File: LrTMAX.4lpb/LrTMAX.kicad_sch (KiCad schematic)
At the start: 126 parts, among them J1 USB_C_Receptacle_USB2.0, J2 Conn_02x05_Odd_Even, Q1 2N7002, SW1 Tact_SW_8mm, SW10 EC11_SMD, SW11 EC11_SMD, SW12 EC11_SMD, SW13 EC11_SMD, SW14 EC11_SMD, SW15 EC11_SMD, SW16 EC11_SMD, SW17 EC11_SMD, SW2 Tact_SW_8mm, SW3 Tact_SW_8mm, SW4 Tact_SW_8mm, SW5 Tact_SW_8mm, SW6 Tact_SW_8mm, SW7 Tact_SW_8mm, SW8 Tact_SW_8mm, U1 STM32F072C8Tx, U3 SSD1306_OLED_0.91, U4 SPX3819M5-L3-3TR

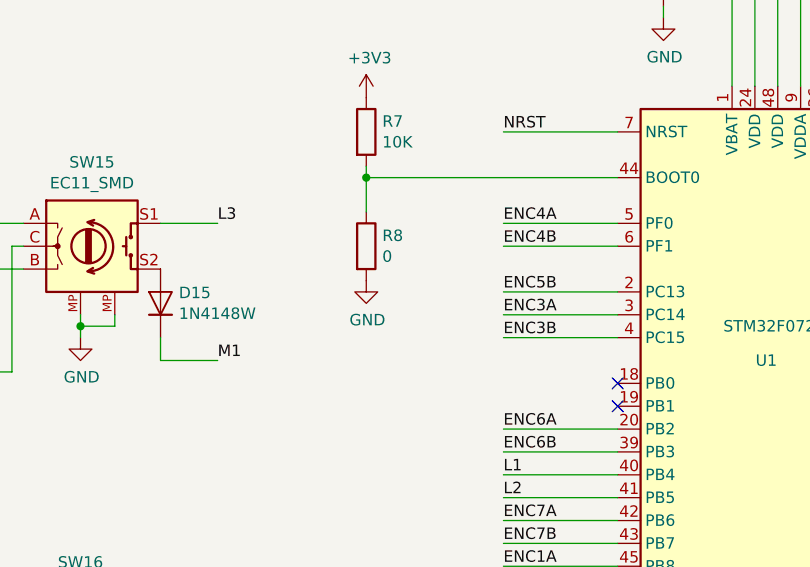
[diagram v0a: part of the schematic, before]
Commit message: Added DFU DIP Switch.
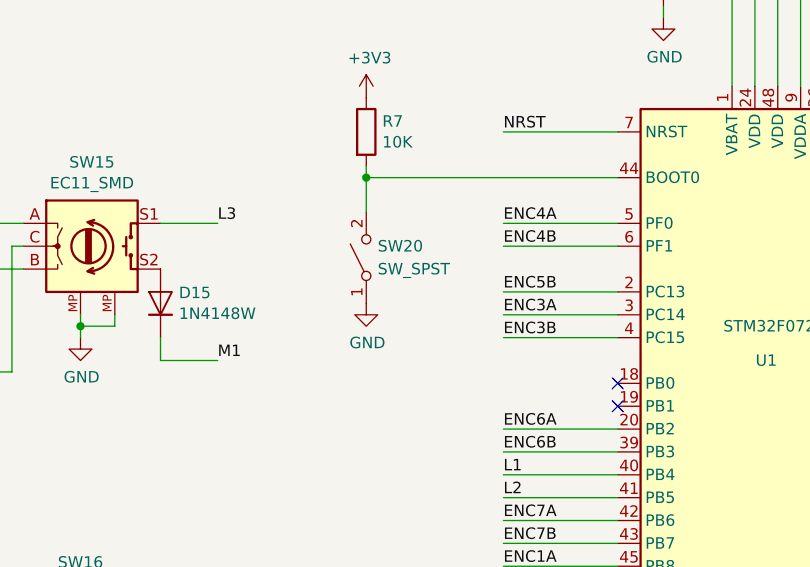
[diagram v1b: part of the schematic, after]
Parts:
- removed R8: 0, Resistor_SMD:R_0805_2012Metric, symbol Device:R
- added SW20: SW_SPST, Button_Switch_SMD:SW_DIP_SPSTx01_Slide_Copal_CHS-01B_W7.62mm_P1.27mm, symbol Switch:SW_SPST
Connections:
- net GND: now also SW20.1 (A)
- net at R7.2, U1.44 (BOOT0): now also SW20.2 (B)
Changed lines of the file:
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@@
     (pin "2")
   )
-  (symbol (lib_id "LrE-6-rescue:GND-power") (at 170.18 83.82 0) (unit 1)
-    (in_bom yes) (on_board yes)
-    (property "Reference" "#PWR0141" (id 0) (at 170.18 90.17 0)
-      (effects (font (size 1.27 1.27)) hide)
-    )
-    (property "Value" "GND" (id 1) (at 170.307 88.2142 0))
-    (property "Footprint" "" (id 2) (at 170.18 83.82 0)
-      (effects (font (size 1.27 1.27)) hide)
-    )
-    (property "Datasheet" "" (id 3) (at 170.18 83.82 0)
+  (symbol (lib_id "LrE-6-rescue:GND-power") (at 170.18 86.36 0) (unit 1)
+    (in_bom yes) (on_board yes)
+    (property "Reference" "#PWR0141" (id 0) (at 170.18 92.71 0)
+      (effects (font (size 1.27 1.27)) hide)
+    )
+    (property "Value" "GND" (id 1) (at 170.307 90.7542 0))
+    (property "Footprint" "" (id 2) (at 170.18 86.36 0)
+      (effects (font (size 1.27 1.27)) hide)
+    )
+    (property "Datasheet" "" (id 3) (at 170.18 86.36 0)
       (effects (font (size 1.27 1.27)) hide)
     )
@@
     (pin "1")
   )
-  (symbol (lib_id "Device:R") (at 170.18 80.01 0) (unit 1)
-    (in_bom yes) (on_board yes)
-    (property "Reference" "R8" (id 0) (at 171.958 78.8416 0)
-      (effects (font (size 1.27 1.27)) (justify left))
-    )
-    (property "Value" "0" (id 1) (at 171.958 81.153 0)
-      (effects (font (size 1.27 1.27)) (justify left))
-    )
-    (property "Footprint" "Resistor_SMD:R_0805_2012Metric" (id 2) (at 168.402 80.01 90)
-      (effects (font (size 1.27 1.27)) hide)
-    )
-    (property "Datasheet" "~" (id 3) (at 170.18 80.01 0)
-      (effects (font (size 1.27 1.27)) hide)
-    )
-    (pin "1")
-    (pin "2")
-  )
   (symbol (lib_id "Device:R") (at 170.18 67.31 0) (unit 1)
     (in_bom yes) (on_board yes)
@@
     (pin "9")
   )
+  (symbol (lib_id "Switch:SW_SPST") (at 170.18 81.28 90) (unit 1)
+    (in_bom yes) (on_board yes) (fields_autoplaced)
+    (property "Reference" "SW20" (id 0) (at 171.45 80.0099 90)
+      (effects (font (size 1.27 1.27)) (justify right))
+    )
+    (property "Value" "SW_SPST" (id 1) (at 171.45 82.5499 90)
+      (effects (font (size 1.27 1.27)) (justify right))
+    )
+    (property "Footprint" "Button_Switch_SMD:SW_DIP_SPSTx01_Slide_Copal_CHS-01B_W7.62mm_P1.27mm" (id 2) (at 170.18 81.28 0)
+      (effects (font (size 1.27 1.27)) hide)
+    )
+    (property "Datasheet" "~" (id 3) (at 170.18 81.28 0)
+      (effects (font (size 1.27 1.27)) hide)
+    )
+    (pin "1")
+    (pin "2")
+  )
   (symbol (lib_id "LrE-6-rescue:+3V3-power") (at 316.23 97.79 0) (unit 1)
     (in_bom yes) (on_board yes)
@@
       (reference "R7") (unit 1) (value "10K") (footprint "Resistor_SMD:R_0805_2012Metric")
     )
-    (path "/00000000-0000-0000-0000-000063d44d4b"
-      (reference "R8") (unit 1) (value "0") (footprint "Resistor_SMD:R_0805_2012Metric")
-    )
     (path "/00000000-0000-0000-0000-00005c6ac614"
       (reference "R10") (unit 1) (value "10K") (footprint "Resistor_SMD:R_0805_2012Metric")
@@
       (reference "SW17") (unit 1) (value "EC11_SMD") (footprint "Rotary_Encoder:RotaryEncoder_Alps_EC11E-Switch_Vertical_H20mm")
     )
+    (path "/a5f04c51-ab64-4878-95f1-94fe64642aaa"
+      (reference "SW20") (unit 1) (value "SW_SPST") (footprint "Button_Switch_SMD:SW_DIP_SPSTx01_Slide_Copal_CHS-01B_W7.62mm_P1.27mm")
+    )
     (path "/00000000-0000-0000-0000-00005c9cf623"

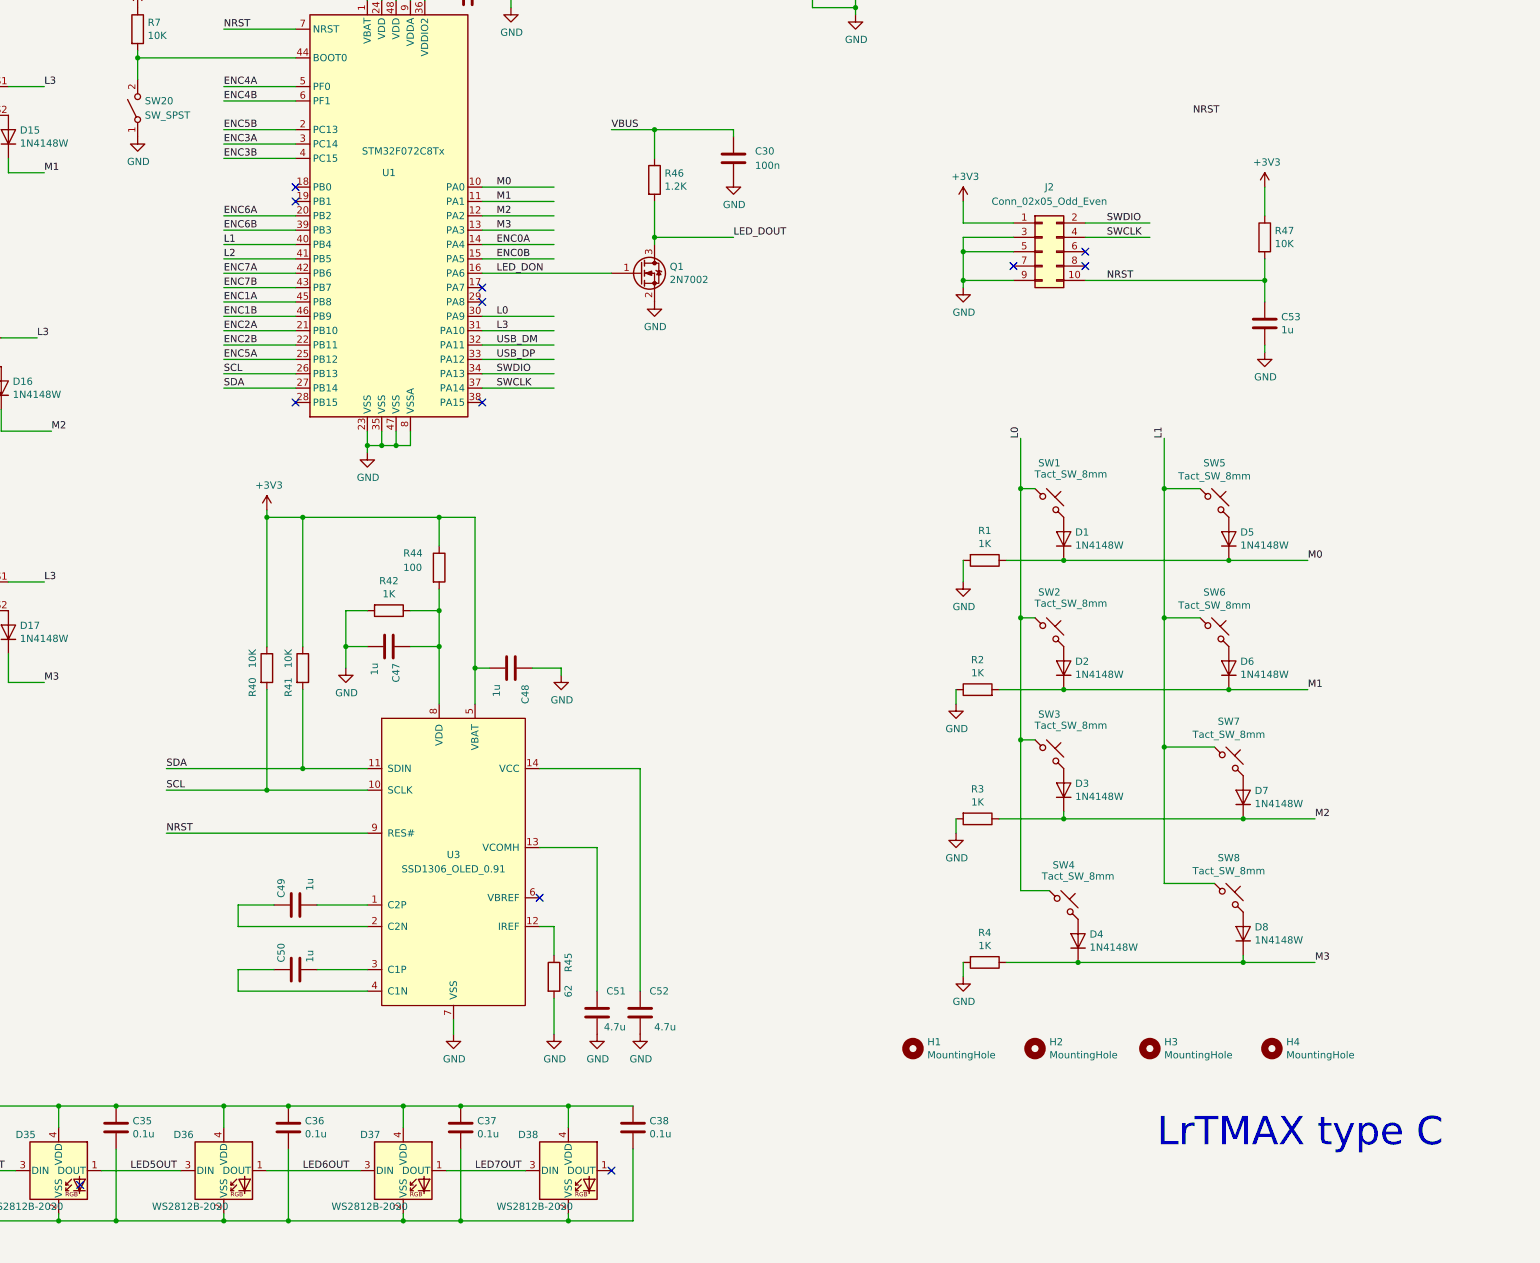
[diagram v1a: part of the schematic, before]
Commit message: Flex wire hall refined
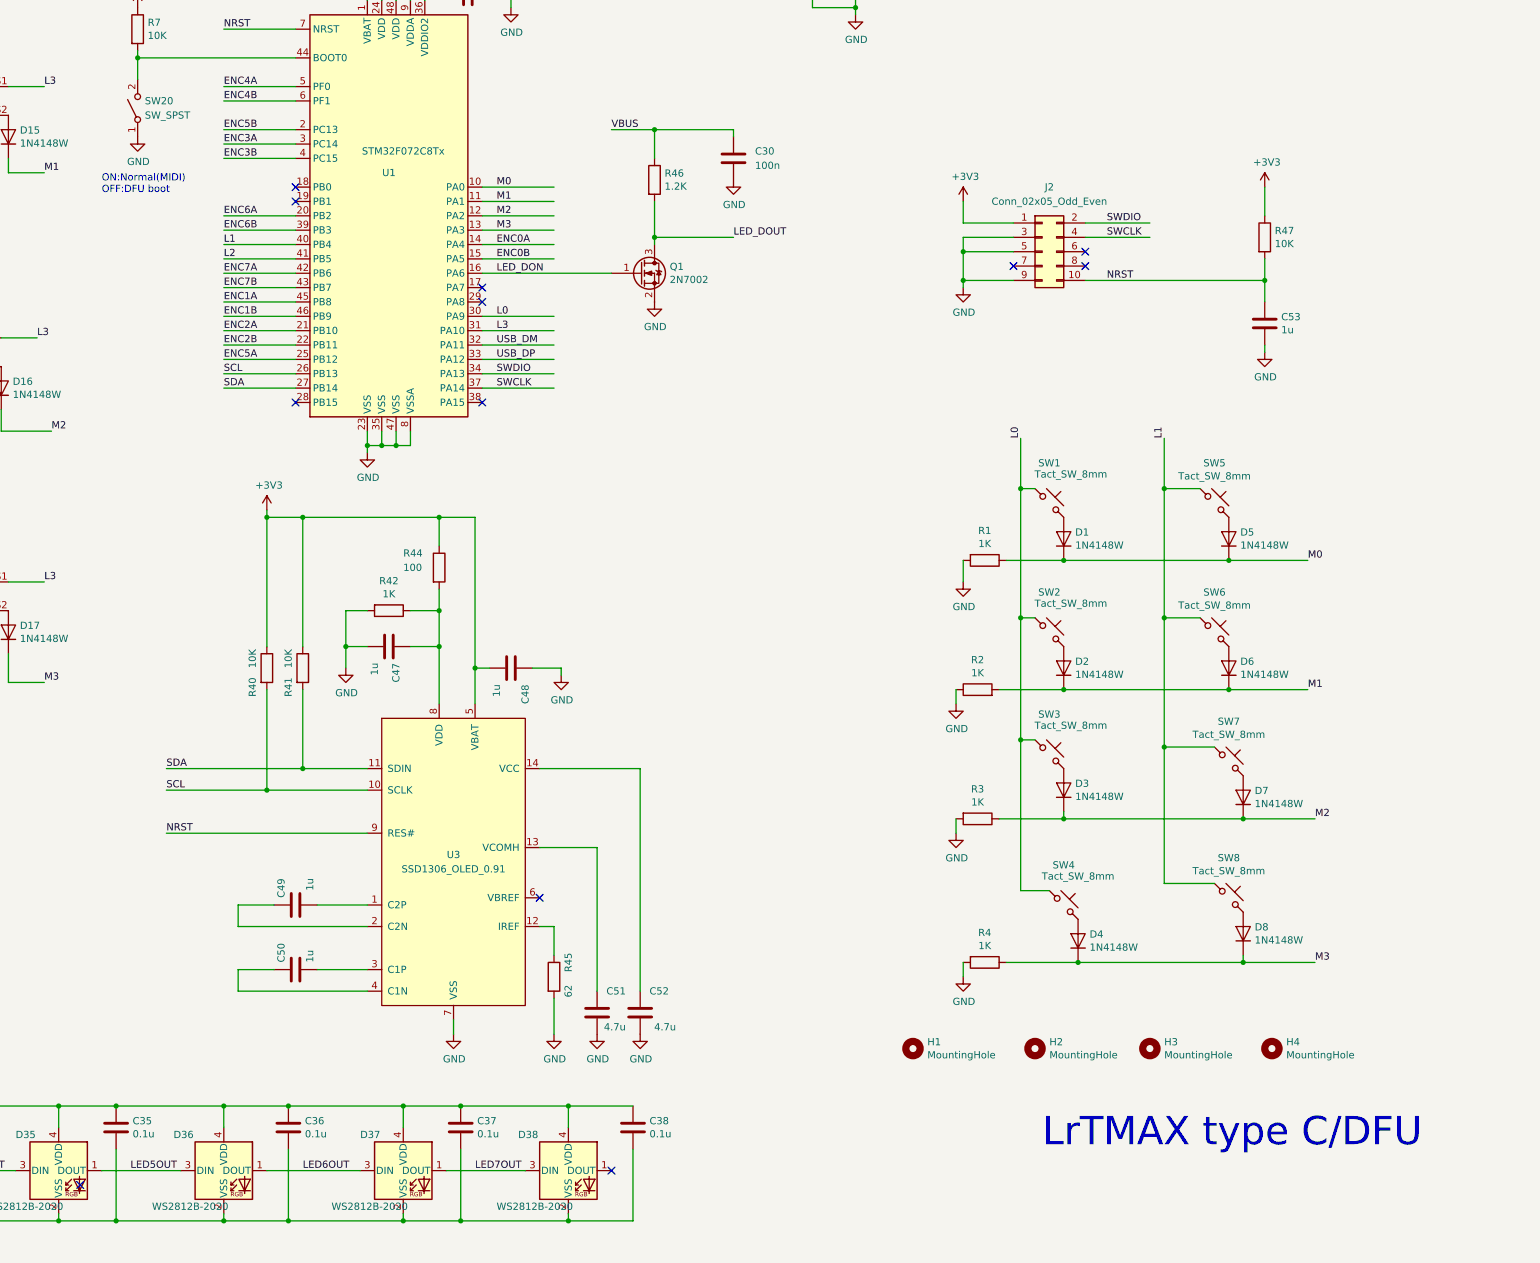
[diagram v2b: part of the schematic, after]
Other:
- note added: "LrTMAX type C/DFU"
- note added: "ON:Normal(MIDI) OFF:DFU boot"
- note removed: "LrTMAX type C"
- title: LrTMAX -> LrTMAX 1.2d
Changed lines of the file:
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@@
   (paper "A3")
   (title_block
-    (title "LrTMAX")
+    (title "LrTMAX 1.2d")
     (date "2019-01-24")
     (company "Ruffles Inc,.")
@@
     (stroke (width 0) (type default) (color 0 0 0 0))
   )
-  (text "LrTMAX type C" (at 350.52 265.43 0)
+  (text "LrTMAX type C/DFU" (at 330.2 265.43 0)
     (effects (font (size 5.0038 5.0038)) (justify left bottom))
   )
+  (text "ON:Normal(MIDI)\nOFF:DFU boot" (at 163.83 96.52 0)
+    (effects (font (size 1.27 1.27)) (justify left bottom))
+  )
   (label "M0" (at 157.48 52.07 0)
     (effects (font (size 1.27 1.27)) (justify left bottom))
@@
     (effects (font (size 1.27 1.27)) (justify left bottom))
   )
-  (label "NRST" (at 356.87 82.55 0)
-    (effects (font (size 1.27 1.27)) (justify left bottom))
-  )
